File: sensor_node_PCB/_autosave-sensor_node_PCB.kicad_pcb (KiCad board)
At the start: 2 copper layers, 97.8 x 49 mm, 49 parts, among them J1 USB_B_Mini, J3 OUTPUT_CONNECTOR, P1 BREAKOUTS, Q1 FDN340P, Q2 BSS138, Q3 BSS138, U1 LMV358IDGKR, U10 dps310, U2 LD1117S50TR, U3 FT231XS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

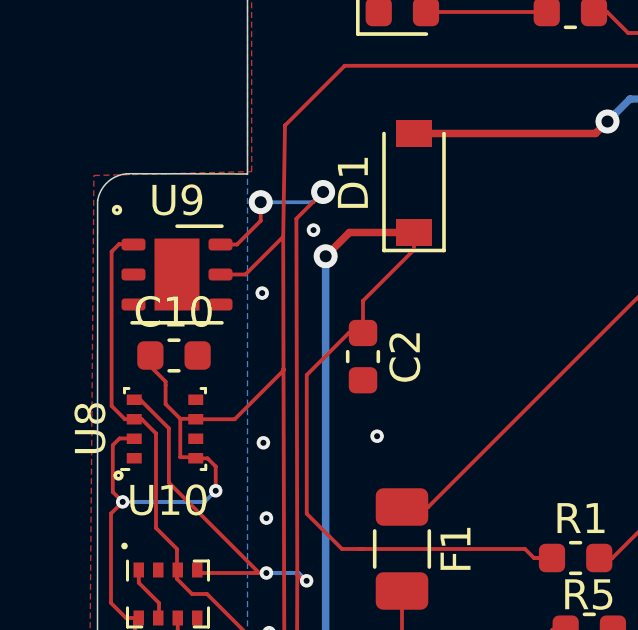
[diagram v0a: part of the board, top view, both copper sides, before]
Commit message: changed usb ic to cp2102 on schematic
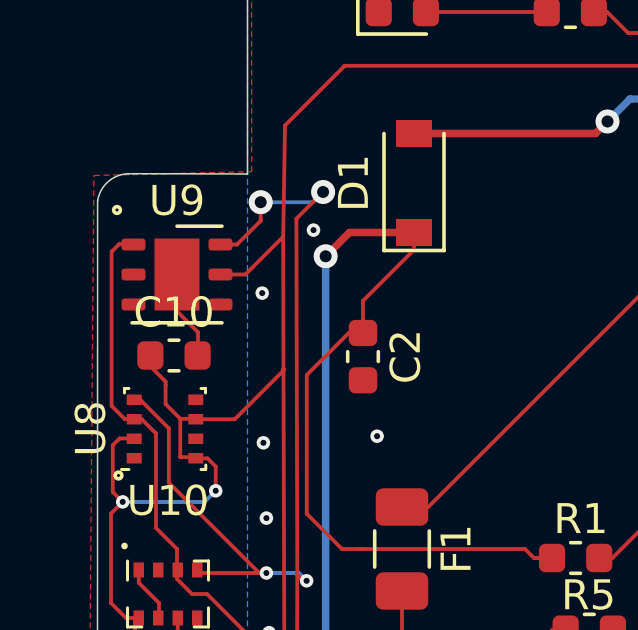
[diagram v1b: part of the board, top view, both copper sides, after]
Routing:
- net GND: track 1.88 -> 4.87 mm
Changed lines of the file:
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@@
     (thickness 1.6)
     (drawings 41)
-    (tracks 566)
+    (tracks 569)
     (zones 0)
     (modules 49)
@@
   (segment (start 103.625 113.625) (end 104.3 114.3) (width 0.127) (layer F.Cu) (net 2))
   (segment (start 104.3 114.3) (end 104.3 114.8) (width 0.127) (layer F.Cu) (net 2))
+  (segment (start 104.9 103.35) (end 104.9 104.575) (width 0.127) (layer F.Cu) (net 2))
+  (segment (start 104.9 104.575) (end 105.6 105.275) (width 0.127) (layer F.Cu) (net 2))
+  (segment (start 105.6 105.275) (end 105.6 106.05) (width 0.127) (layer F.Cu) (net 2))
   (segment (start 116.9625 112.8) (end 117.4 112.8) (width 0.127) (layer F.Cu) (net 3) (status 30))
   (segment (start 116.8 112.8) (end 116.9625 112.8) (width 0.127) (layer F.Cu) (net 3) (status 20))
